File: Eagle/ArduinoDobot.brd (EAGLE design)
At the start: 160 x 100 mm, 10 parts, among them X1 057-010-1

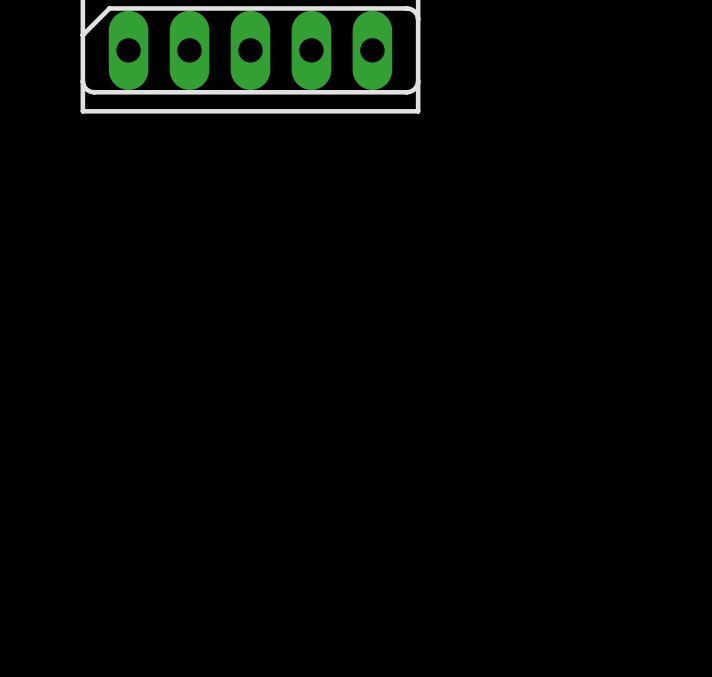
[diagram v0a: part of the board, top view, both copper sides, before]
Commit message: demo button added
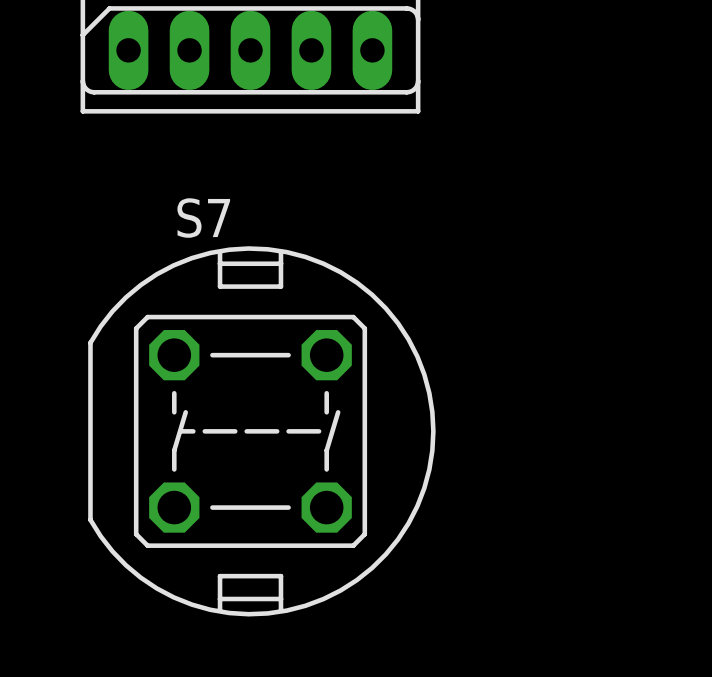
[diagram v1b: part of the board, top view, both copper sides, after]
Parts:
- added S7: DTE6, switch-misc:DTE6
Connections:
- removed net SW: JOYSTICK.5, U$1.GND@7
- new net N$2: S7.3, U$1.32
- net GND2: now also JOYSTICK.5, S7.1, U$1.GND@7; no longer U$1.GND@4
- net N$1: now also U$1.48; no longer U$1.50
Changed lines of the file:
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@@
 <attribute name="VALUE" x="0.762" y="-110.236" size="1.27" layer="27" ratio="10"/>
+</element>
+<element name="S7" library="switch-misc" library_urn="urn:adsk.eagle:library:376" package="DTE6" package3d_urn="urn:adsk.eagle:package:27432/1" value="DTE6" x="6.35" y="-119.38" smashed="yes">
+<attribute name="NAME" x="3.81" y="-112.903" size="1.27" layer="25" ratio="10"/>
+<attribute name="POPULARITY" value="0" x="-6.35" y="-101.6" size="1.778" layer="27" display="off"/>
+<attribute name="VALUE" x="3.81" y="-127.127" size="1.27" layer="27" ratio="10"/>
 </element>
 </elements>
@@
 <contactref element="U$1" pad="GND@2"/>
 <contactref element="X1" pad="10"/>
-<contactref element="U$1" pad="GND@4"/>
-<wire x1="99.06" y1="58.42" x2="101.6" y2="82.55" width="0" layer="19" extent="1-1"/>
+<contactref element="U$1" pad="GND@7"/>
+<contactref element="JOYSTICK" pad="5"/>
+<contactref element="S7" pad="1"/>
 <wire x1="63.5" y1="85.09" x2="101.6" y2="82.55" width="0" layer="19" extent="1-1"/>
-<wire x1="45.72" y1="10.16" x2="99.06" y2="58.42" width="0" layer="19" extent="1-1"/>
+<wire x1="101.6" y1="15.24" x2="101.6" y2="82.55" width="0" layer="19" extent="1-1"/>
+<wire x1="45.72" y1="10.16" x2="101.6" y2="15.24" width="0" layer="19" extent="1-1"/>
 <wire x1="3.81" y1="-6.35" x2="45.72" y2="10.16" width="0" layer="19" extent="1-1"/>
 <wire x1="3.81" y1="-24.13" x2="3.81" y2="-6.35" width="0" layer="19" extent="1-1"/>
@@
 <wire x1="3.81" y1="-59.69" x2="3.81" y2="-41.91" width="0" layer="19" extent="1-1"/>
 <wire x1="2.286" y1="-106.68" x2="3.81" y2="-59.69" width="0" layer="19" extent="1-1"/>
+<wire x1="10.414" y1="-106.68" x2="2.286" y2="-106.68" width="0" layer="19" extent="1-1"/>
+<wire x1="3.81" y1="-116.84" x2="2.286" y2="-106.68" width="0" layer="19" extent="1-1"/>
 </signal>
 <signal name="N$1">
-<contactref element="U$1" pad="50"/>
 <contactref element="S1" pad="3"/>
-<wire x1="99.06" y1="20.32" x2="68.58" y2="80.01" width="0" layer="19" extent="1-1"/>
+<contactref element="U$1" pad="48"/>
+<wire x1="99.06" y1="22.86" x2="68.58" y2="80.01" width="0" layer="19" extent="1-1"/>
 </signal>
 <signal name="N$5">
@@
 <wire x1="8.89" y1="-64.77" x2="99.06" y2="15.24" width="0" layer="19" extent="1-1"/>
 </signal>
-<signal name="SW">
-<contactref element="U$1" pad="GND@7"/>
-<contactref element="JOYSTICK" pad="5"/>
-<wire x1="10.414" y1="-106.68" x2="101.6" y2="15.24" width="0" layer="19" extent="1-1"/>
-</signal>
 <signal name="VRY">
 <contactref element="JOYSTICK" pad="4"/>
@@
 <wire x1="3.81" y1="-91.44" x2="8.89" y2="-46.99" width="0" layer="19" extent="1-1"/>
 </signal>
+<signal name="N$2">
+<contactref element="S7" pad="3"/>
+<contactref element="U$1" pad="32"/>
+<wire x1="8.89" y1="-121.92" x2="99.06" y2="43.18" width="0" layer="19" extent="1-1"/>
+</signal>
 </signals>
